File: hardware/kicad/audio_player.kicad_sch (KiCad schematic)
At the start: 35 parts, among them IC1 XC6220B331PR-G, J1 AudioJack3_Switch, J2 Conn_01x06_Pin, SW1 SW_Push, SW2 RotaryEncoder_Switch, SW3 SW_Push, SW4 SW_Push, U1 IP5306-I2C, U2 PCM5102A, U3 TPA6132A2RTE, U5 LicheeRV_Nano, U6 INA219AxD

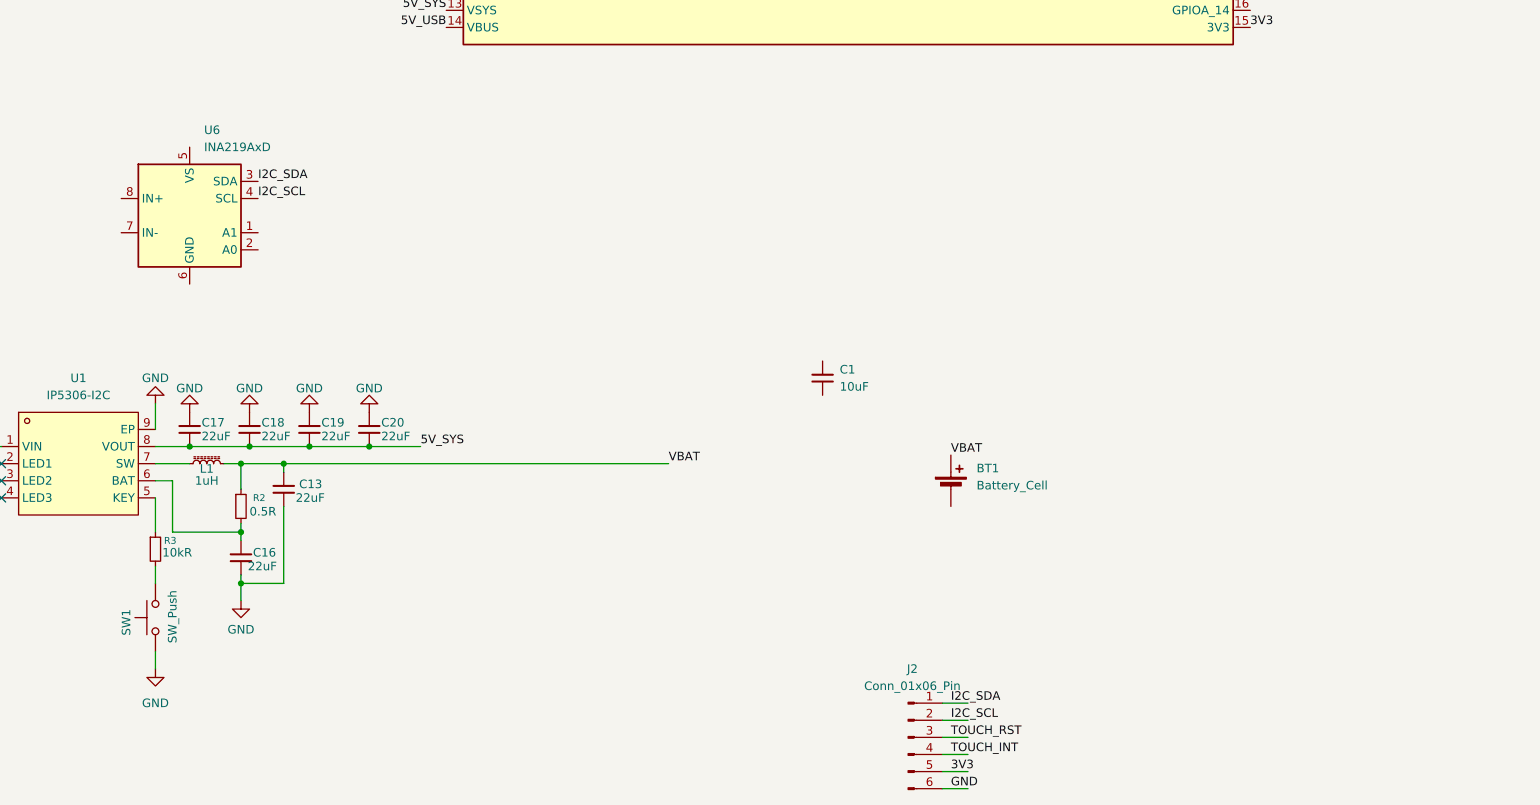
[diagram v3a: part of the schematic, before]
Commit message: kicad_sch(power_system): add INA219AxD peripheral elements
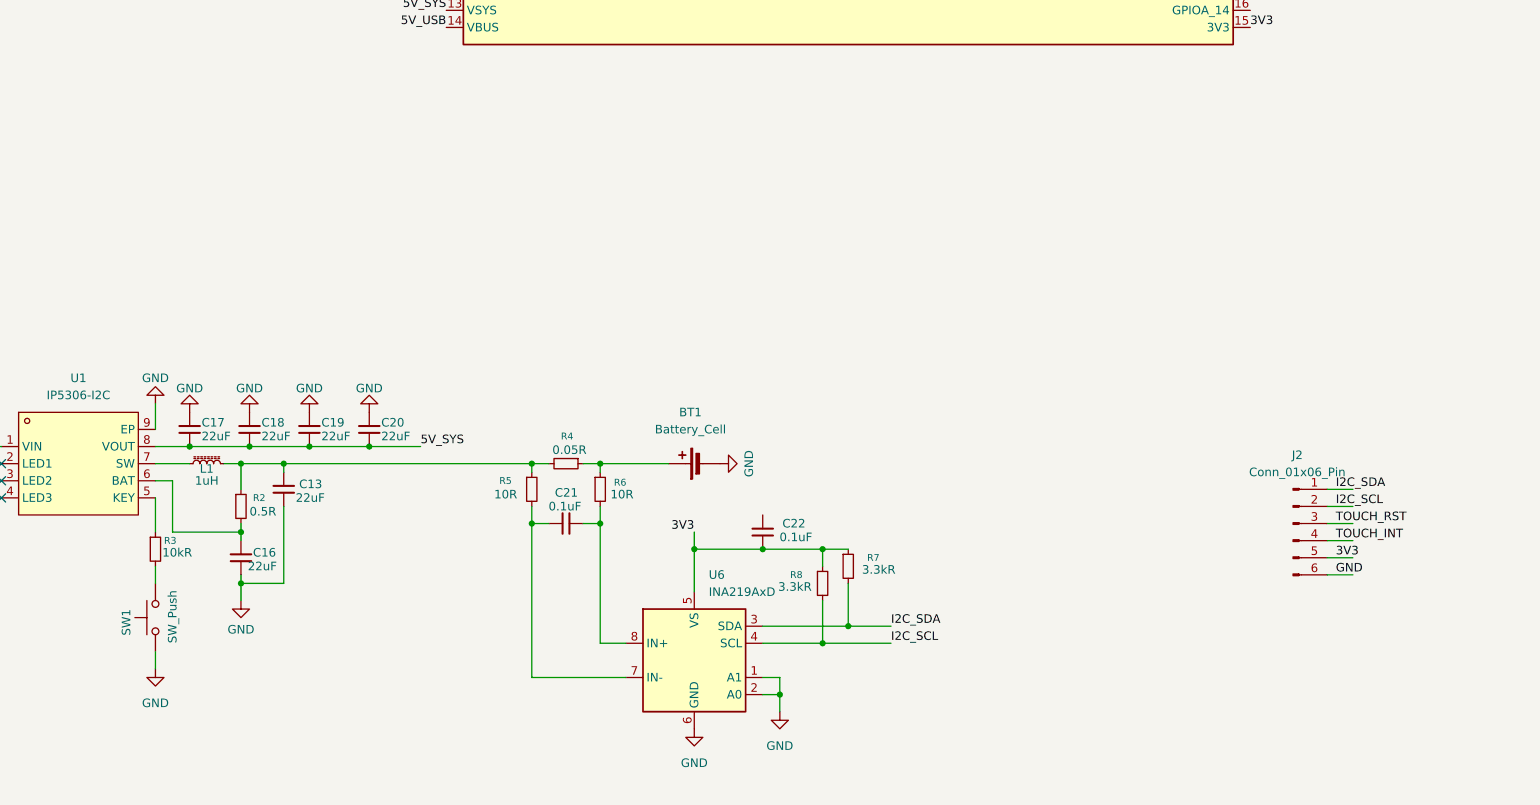
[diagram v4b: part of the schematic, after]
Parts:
- removed C1: 10uF, symbol Device:C_Small
- added C21, C22: 0.1uF, symbol Device:C_Small
- added R4: 0.05R, symbol Device:R_Small
- added R5, R6: 10R, symbol Device:R_Small
- added R7, R8: 3.3kR, symbol Device:R_Small
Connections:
- net 3V3: now also U6.5 (VS), C22.1, R7.1, R8.1
- net GND: now also BT1.2 (-), U6.1 (A1), U6.2 (A0), U6.6 (GND)
- net I2C_SCL: now also R8.2
- net I2C_SDA: now also R7.2
- net at U6.7 (IN-): now also C21.1, R5.2
- net at U6.8 (IN+): now also C21.2, R6.2
- net VBAT: no longer names the net of C13.1, L1.2, R2.1
- net VBAT: now also R4.2, R5.1; no longer BT1.1 (+)
- new net: BT1.1 (+), R4.1, R6.1
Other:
- moved on the sheet: BT1, J2, U6

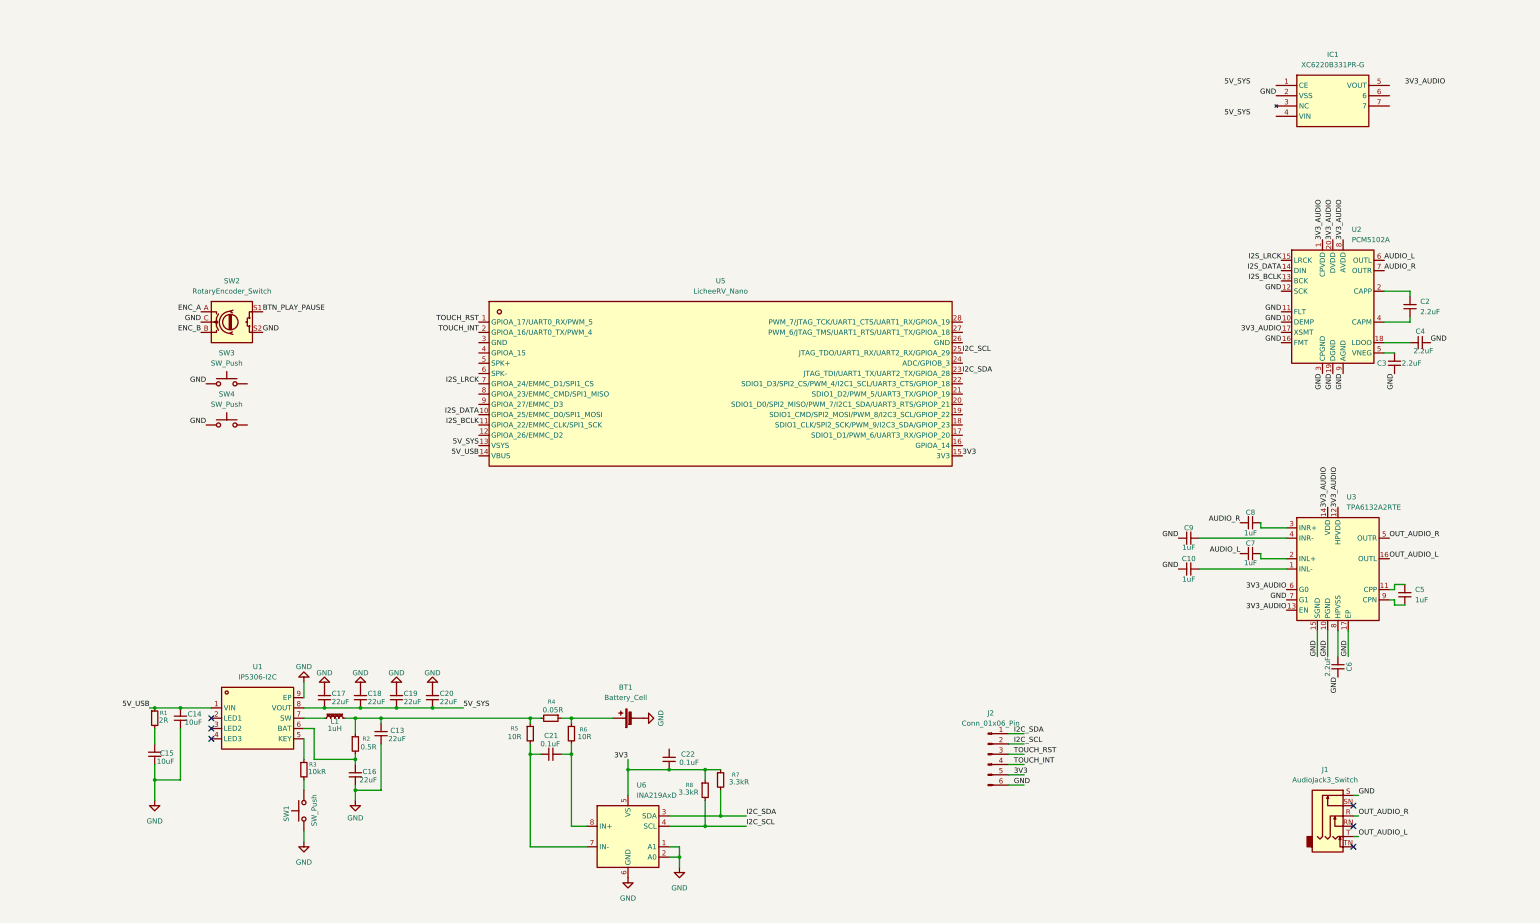
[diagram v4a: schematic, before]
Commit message: kicad_sch(power_system): moved pull up i2c to main device + add peripheral elements to audio LDO
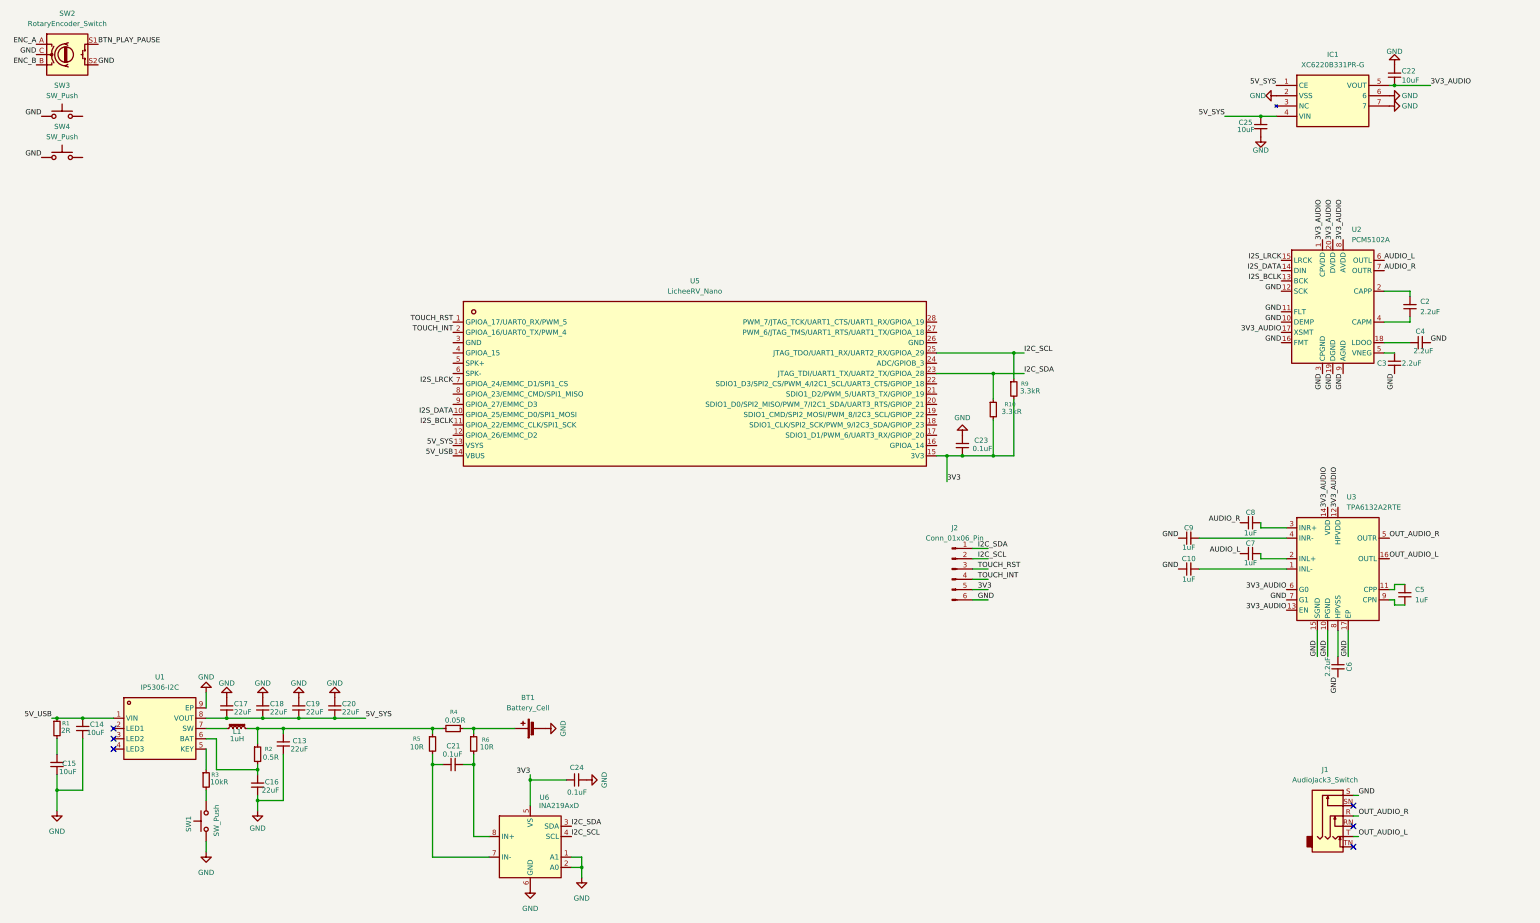
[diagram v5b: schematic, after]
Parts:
- removed R7, R8: 3.3kR, symbol Device:R_Small
- added C23, C24: 0.1uF, symbol Device:C_Small
- added C25: 10uF, symbol Device:C_Small
- added R10, R9: 3.3kR, symbol Device:R_Small
- C22: value 0.1uF -> 10uF
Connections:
- net 3V3: now also C23.1, C24.1, R10.2, R9.2; no longer C22.1
- net 3V3_AUDIO: now also C22.2, IC1.5 (VOUT)
- net 5V_SYS: now also IC1.1 (CE), IC1.4 (VIN), C25.2
- net GND: now also C22.1, IC1.6, IC1.7, C23.2, C24.2, C25.1
- net I2C_SCL: now also R9.1
- net I2C_SDA: now also R10.1
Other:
- moved on the sheet: BT1, C13, C14, C15, C16, C17, C18, C19, C20, C21, J2, L1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

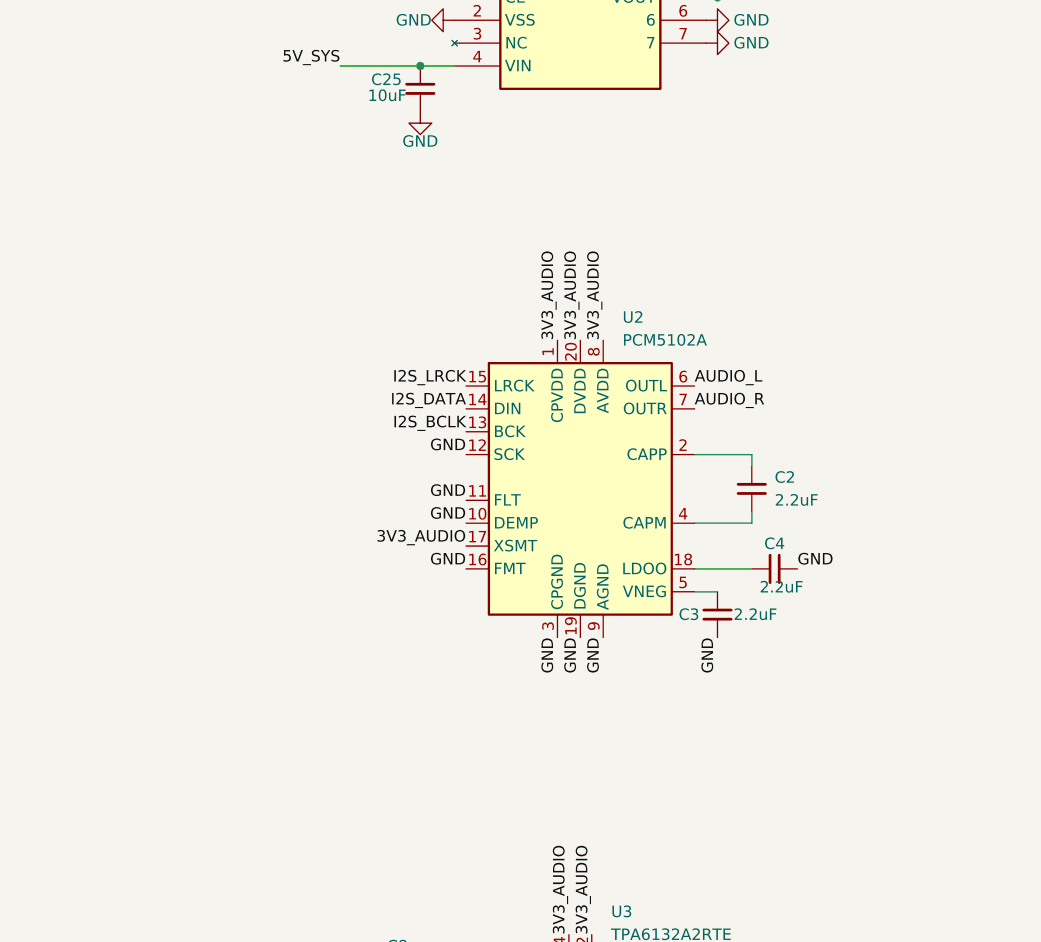
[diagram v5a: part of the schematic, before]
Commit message: kicad_sch(audio_system): add peripheral for PCM5102A dac
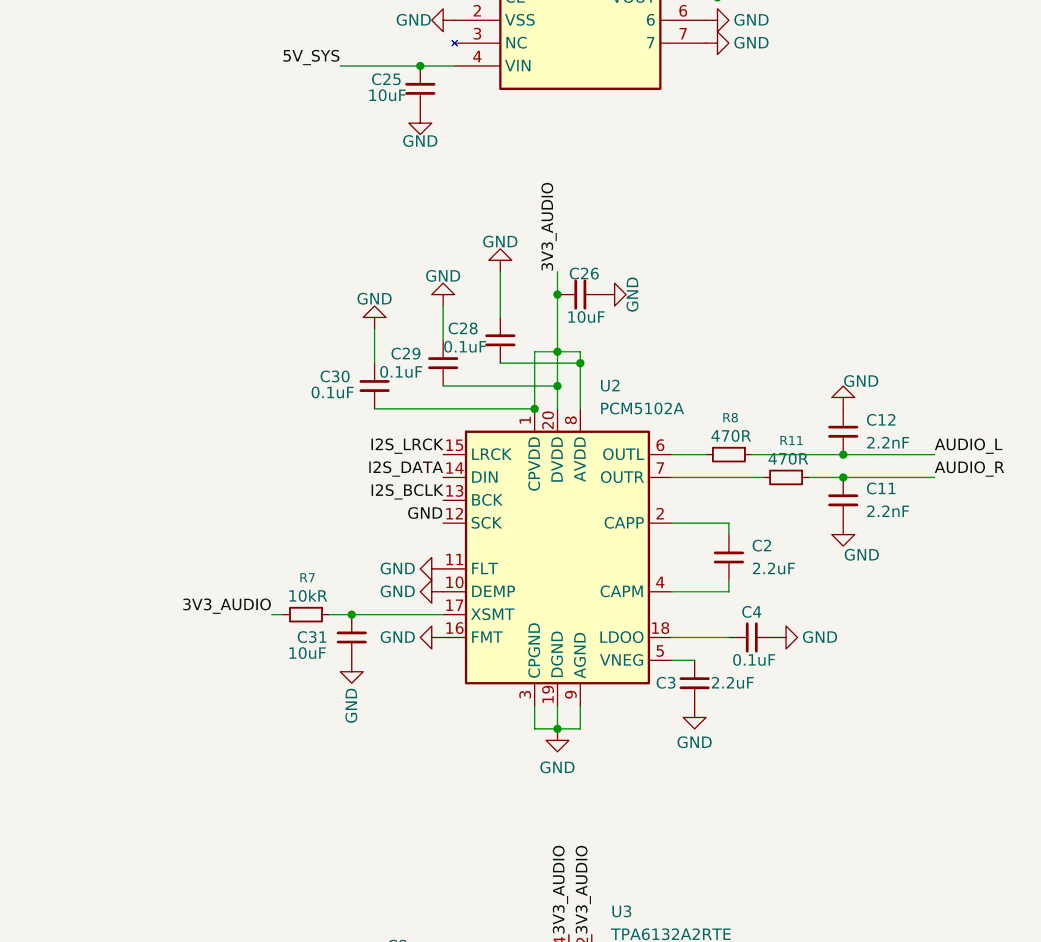
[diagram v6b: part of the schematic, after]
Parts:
- added C11, C12: 2.2nF, RF_Module:Jadak_Thingmagic_M6e-Nano, symbol Device:C_Small
- added C26, C31: 10uF, symbol Device:C_Small
- added C28, C29, C30: 0.1uF, symbol Device:C_Small
- added R11, R8: 470R, symbol Device:R_Small
- added R7: 10kR, symbol Device:R_Small
- C4: value 2.2uF -> 0.1uF
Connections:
- net 3V3_AUDIO: now also C26.2, C28.2, C29.2, C30.2, R7.2; no longer U2.17 (XSMT)
- net AUDIO_L: now also C12.2, R8.1; no longer U2.6 (OUTL)
- net AUDIO_R: now also C11.1, R11.1; no longer U2.7 (OUTR)
- net GND: now also C11.2, C12.1, C26.1, C28.1, C29.1, C30.1, C31.2
- new net: R8.2, U2.6 (OUTL)
- new net: C31.1, R7.1, U2.17 (XSMT)
- new net: R11.2, U2.7 (OUTR)
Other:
- moved on the sheet: C2, C3, C4, U2
